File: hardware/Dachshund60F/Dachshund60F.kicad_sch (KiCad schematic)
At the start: 203 parts, among them J1 USB daughterboard (JST-SH 4P), J2 Battery (JST-PH 2P), J3 SWD, SW1 Power, SW100 MX Esc (1.00u), SW101 MX F1 (1.00u), SW102 MX F2 (1.00u), SW103 MX F3 (1.00u), SW104 MX F4 (1.00u), SW105 MX F5 (1.00u), SW106 MX F6 (1.00u), SW107 MX F7 (1.00u), SW108 MX F8 (1.00u), SW109 MX F9 (1.00u), SW110 MX F10 (1.00u), SW111 MX F11 (1.00u), SW112 MX F12 (1.00u), SW113 MX Delete (1.00u), SW2 Reset, SW200 MX ` (1.00u), SW201 MX 1 (1.00u), SW202 MX 2 (1.00u), SW203 MX 3 (1.00u), SW204 MX 4 (1.00u), SW205 MX 5 (1.00u), SW206 MX 6 (1.00u), SW207 MX 7 (1.00u), SW208 MX 8 (1.00u), SW209 MX 9 (1.00u), SW210 MX 0 (1.00u), SW211 MX - (1.00u), SW212 MX = (1.00u), SW213 MX Backspace (2.00u), SW3 PEC12R-4220F-S0024 (horizonta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, SW300 MX Tab (1.50u), SW301 MX Q (1.00u), SW302 MX W (1.00u), SW303 MX E (1.00u), SW304 MX R (1.00u), SW305 MX T (1.00u), SW306 MX Y (1.00u), SW307 MX U (1.00u), SW308 MX I (1.00u), SW309 MX O (1.00u), SW310 MX P (1.00u), SW311 MX [ (1.00u), SW312 MX ] (1.00u), SW313 MX \ (1.50u), SW400 MX Caps Lock (1.75u), SW401 MX A (1.00u), SW402 MX S (1.00u), SW403 MX D (1.00u), SW404 MX F (1.00u), SW405 MX G (1.00u), SW406 MX H (1.00u), SW407 MX J (1.00u), SW408 MX K (1.00u), SW409 MX L (1.00u), SW410 MX ; (1.00u), SW411 MX ' (1.00u), SW413 MX Enter (2.25u), SW500 MX Shift (2.25u), SW501 MX Z (1.00u), SW502 MX X (1.00u), SW503 MX C (1.00u), SW504 MX V (1.00u), SW505 MX B (1.00u), SW506 MX N (1.00u), SW507 MX M (1.00u), SW508 MX , (1.00u), SW509 MX . (1.00u), SW510 MX / (1.00u), SW512 MX Shift (1.75u), SW513 MX Up (1.00u), SW600 MX Ctrl (1.25u), SW601 MX Win (1.25u), SW603 MX Alt (1.25u), SW604 MX Mod (1.25u, solder), SW606 MX Space full (6.25u, solder), SW608 MX Mod (2.25u)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

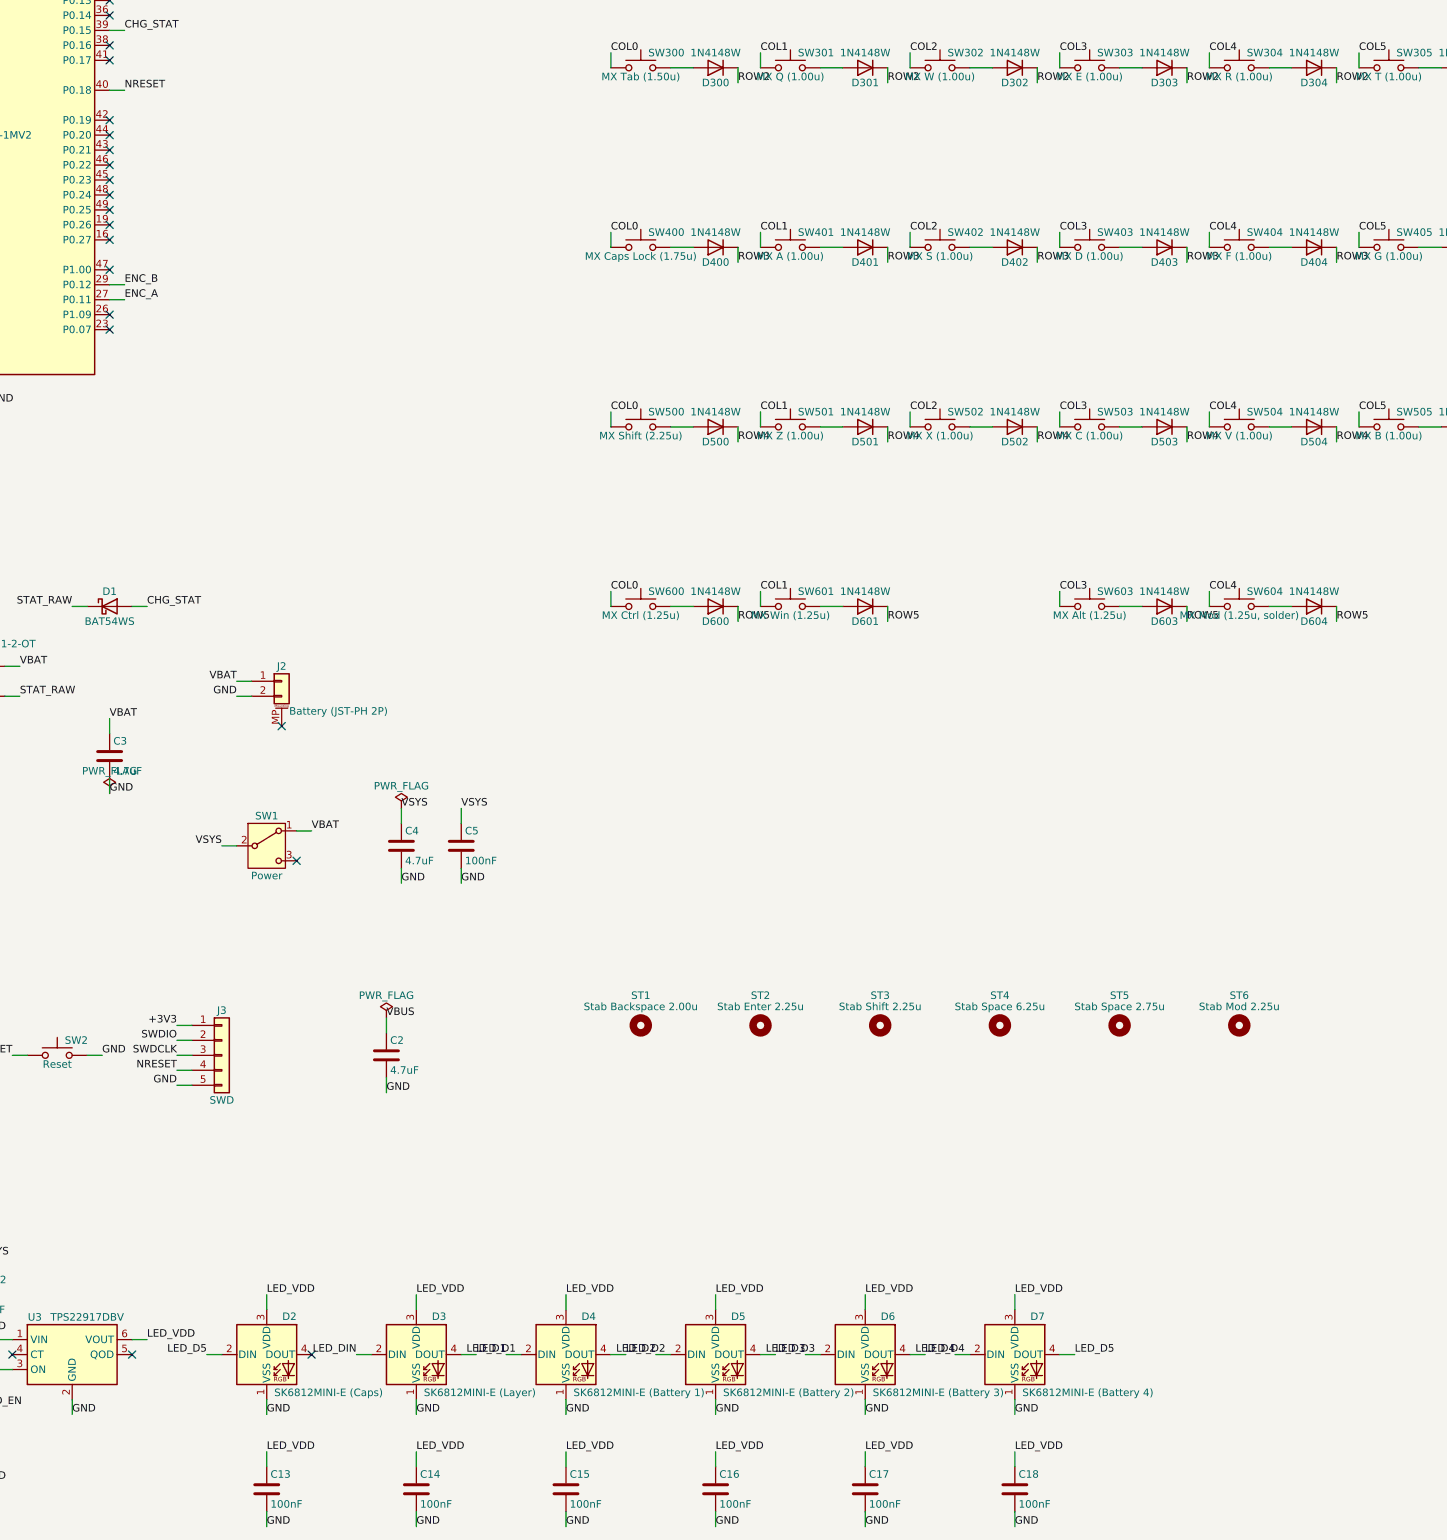
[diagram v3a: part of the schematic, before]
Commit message: Add display header J4 to Dachshund60F
An 8-pin 2.54 mm through-hole header on the front at y 112.5 mm, between
the reset button and the LED load switch, for a case-mounted e-ink or
OLED display. Pinout in Waveshare e-Paper module order: +3V3, GND,
DIN (P0.21), CLK (P0.19), CS (P0.20), DC (P0.23), RST (P0.22),
BUSY (P0.24); an I2C OLED uses CLK/DIN as SCL/SDA. Pin names are on the
front silkscreen. Power is +3V3 straight from REGOUT0.

- Re-route the board. DRC: 0 errors and 0 unconnected items, besides the
  7 excluded spacebar items. Nothing is in the antenna keep-out.
- board.json: new display section; the host-lib pin test covers it.
- Hardware provision only: SPEC.md still lists the display as not in v1.

Co-Authored-By: Claude Opus 5.5 <noreply@anthropic.com>
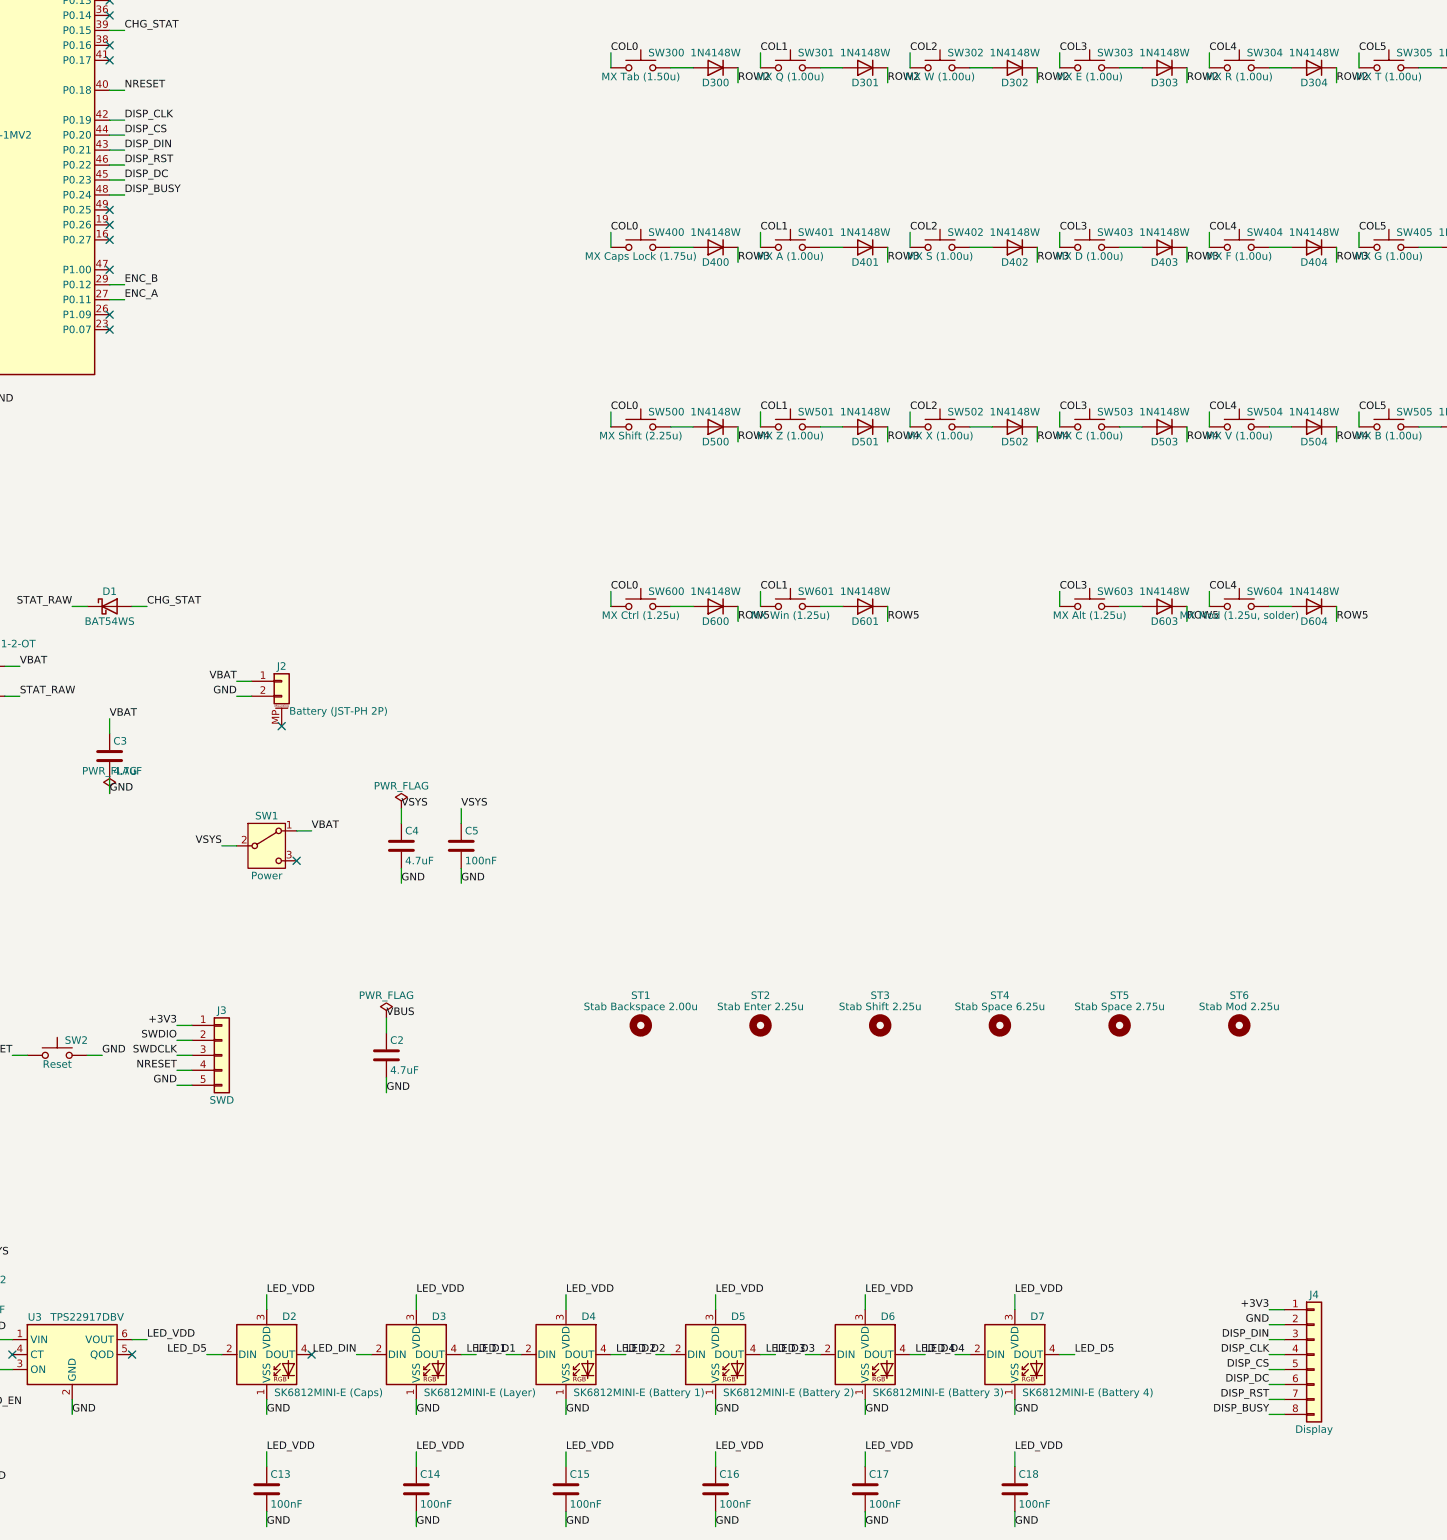
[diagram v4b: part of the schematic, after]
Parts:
- added J4: Display, Connector_PinHeader_2.54mm:PinHeader_1x08_P2.54mm_Vertical, symbol Connector_Generic:Conn_01x08
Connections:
- net +3V3: now also J4.1 (Pin_1)
- net GND: now also J4.2 (Pin_2)
- net DISP_CLK: now reaches U1.42 (P0.19)
- net DISP_CLK: now also J4.4 (Pin_4)
- net DISP_DIN: now reaches U1.43 (P0.21)
- net DISP_DIN: now also J4.3 (Pin_3)
- net DISP_CS: now reaches U1.44 (P0.20)
- net DISP_CS: now also J4.5 (Pin_5)
- net DISP_DC: now reaches U1.45 (P0.23)
- net DISP_DC: now also J4.6 (Pin_6)
- net DISP_RST: now reaches U1.46 (P0.22)
- net DISP_RST: now also J4.7 (Pin_7)
- net DISP_BUSY: now reaches U1.48 (P0.24)
- net DISP_BUSY: now also J4.8 (Pin_8)
- no-connect marks 25 -> 19

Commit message: Add the FR4 gasket plate; give the LED cutouts more clearance
Plate (hardware/Dachshund60F-Plate): generated from the mainboard by
gen_plate.py, run with KiCad's Python. 1.6 mm FR4 with cutouts for 80
switches and 12 Cherry stabilizers (both spacebar layouts, overlaps
merged), an encoder notch, a J4 slot and windows over D3-D7. Eight
2.8 x 6.5 mm tabs take silicone gasket socks. Exposed-copper accent
rings follow every switch and stabilizer cutout, at least 0.4 mm from
any routed edge. DRC: 0 violations.

Mainboard: D2-D7 use a project copy of the SK6812MINI-E reverse-mount
footprint with a plain 3.4 x 3.4 mm cutout instead of the corner
reliefs. Pads are now 0.35 mm from the edge (was 0.247 mm), and the
LED cutout DRC rule is raised from 0.2 mm to 0.3 mm. ERC 0, DRC 0
errors after the zone refill.

Co-Authored-By: Claude Opus 5.5 <noreply@anthropic.com>
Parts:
- D2, D3, D4, D5, D6, D7: footprint LED_SMD:LED_SK6812MINI-E_3.2x2.8mm_P1.5mm_ReverseMount -> Dachshund60F:LED_SK6812MINI-E_3.2x2.8mm_P1.5mm_ReverseMount_Cutout3.4
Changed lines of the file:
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@@
 			)
 		)
-		(property "Footprint" "LED_SMD:LED_SK6812MINI-E_3.2x2.8mm_P1.5mm_ReverseMount"
+		(property "Footprint" "Dachshund60F:LED_SK6812MINI-E_3.2x2.8mm_P1.5mm_ReverseMount_Cutout3.4"
 			(at 127 330.2 0)
 			(hide yes)
@@
 			)
 		)
-		(property "Footprint" "LED_SMD:LED_SK6812MINI-E_3.2x2.8mm_P1.5mm_ReverseMount"
+		(property "Footprint" "Dachshund60F:LED_SK6812MINI-E_3.2x2.8mm_P1.5mm_ReverseMount_Cutout3.4"
 			(at 152.4 330.2 0)
 			(hide yes)
@@
 			)
 		)
-		(property "Footprint" "LED_SMD:LED_SK6812MINI-E_3.2x2.8mm_P1.5mm_ReverseMount"
+		(property "Footprint" "Dachshund60F:LED_SK6812MINI-E_3.2x2.8mm_P1.5mm_ReverseMount_Cutout3.4"
 			(at 177.8 330.2 0)
 			(hide yes)
@@
 			)
 		)
-		(property "Footprint" "LED_SMD:LED_SK6812MINI-E_3.2x2.8mm_P1.5mm_ReverseMount"
+		(property "Footprint" "Dachshund60F:LED_SK6812MINI-E_3.2x2.8mm_P1.5mm_ReverseMount_Cutout3.4"
 			(at 203.2 330.2 0)
 			(hide yes)
@@
 			)
 		)
-		(property "Footprint" "LED_SMD:LED_SK6812MINI-E_3.2x2.8mm_P1.5mm_ReverseMount"
+		(property "Footprint" "Dachshund60F:LED_SK6812MINI-E_3.2x2.8mm_P1.5mm_ReverseMount_Cutout3.4"
 			(at 228.6 330.2 0)
 			(hide yes)
@@
 			)
 		)
-		(property "Footprint" "LED_SMD:LED_SK6812MINI-E_3.2x2.8mm_P1.5mm_ReverseMount"
+		(property "Footprint" "Dachshund60F:LED_SK6812MINI-E_3.2x2.8mm_P1.5mm_ReverseMount_Cutout3.4"
 			(at 254 330.2 0)
 			(hide yes)

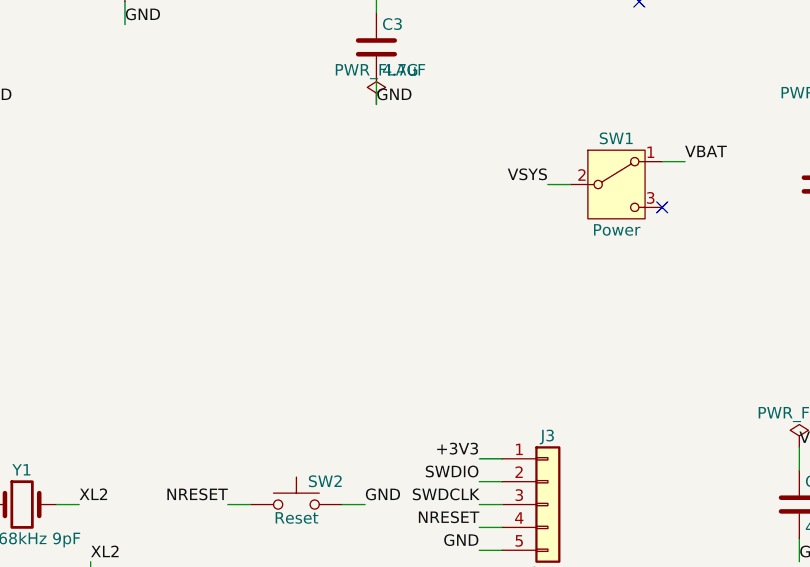
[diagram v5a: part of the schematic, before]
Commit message: Add a USB power path to the mainboard, licences and a task list
The mainboard ran only from the battery through the slide switch, so it
was off on USB with the switch off and browned out with no battery.

- Schematic and PCB: Microchip's MCP73831 load-sharing circuit. SW1 now
  feeds VBAT_SW; Q1 (AO3401A) connects it to VSYS only while VBUS is
  absent, R3 (100k) pulls the gate down, and D8 (B5819W) feeds VSYS from
  VBUS. Placed on the back between J2, J3 and SW1 and hand-routed; ERC
  and DRC show no new errors.
- Licence: MIT for code (LICENSE), CERN-OHL-P-2.0 for hardware
  (hardware/LICENSE).
- SCHEDULED_TASKS.md: open tasks to reference in later prompts.
- Bring-up plan, board README and PROGRESS updated, including the LED
  data margin on USB as an open question.

Co-Authored-By: Claude Opus 5.5 (1M context) <noreply@anthropic.com>
Claude-Session: https://claude.ai/code/session_01D9WgQVzjyM3BLJSpari9iy
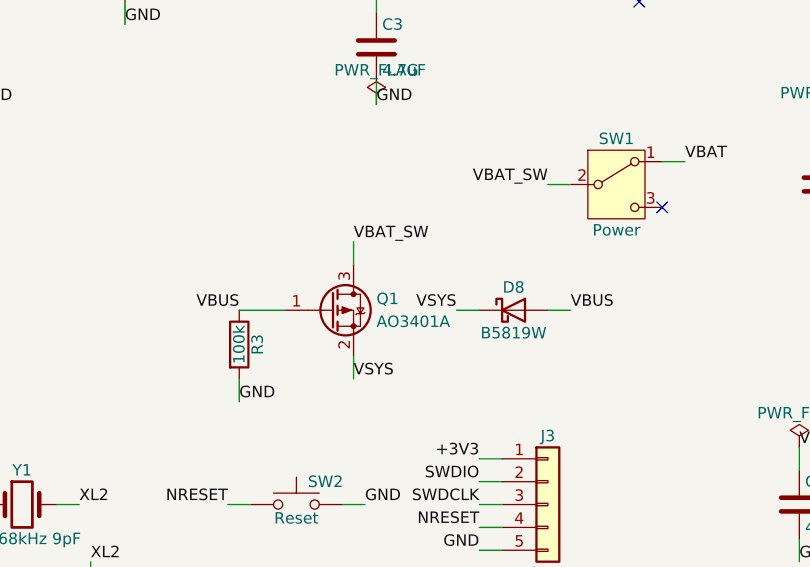
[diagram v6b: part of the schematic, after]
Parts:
- added D8: B5819W, Diode_SMD:D_SOD-123, symbol Device:D_Schottky
- added Q1: AO3401A, Package_TO_SOT_SMD:SOT-23, symbol Transistor_FET:AO3401A
- added R3: 100k, Resistor_SMD:R_0603_1608Metric, symbol Device:R
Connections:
- net GND: now also R3.2
- net VBUS: now also D8.2 (A), Q1.1 (G), R3.1
- net VSYS: now also D8.1 (K), Q1.2 (S); no longer SW1.2 (B)
- new net VBAT_SW: Q1.3 (D), SW1.2 (B)
